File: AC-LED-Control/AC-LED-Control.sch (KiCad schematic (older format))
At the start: 44 parts, among them P101 CONN_01X02, P102 CONN_01X02, P103 CONN_01X04, P104 CONN_01X02, SW101 SW_PUSH, U101 FOD814-D, U102 STM32F030F4P6, U103 74HC595, U104 74HC595

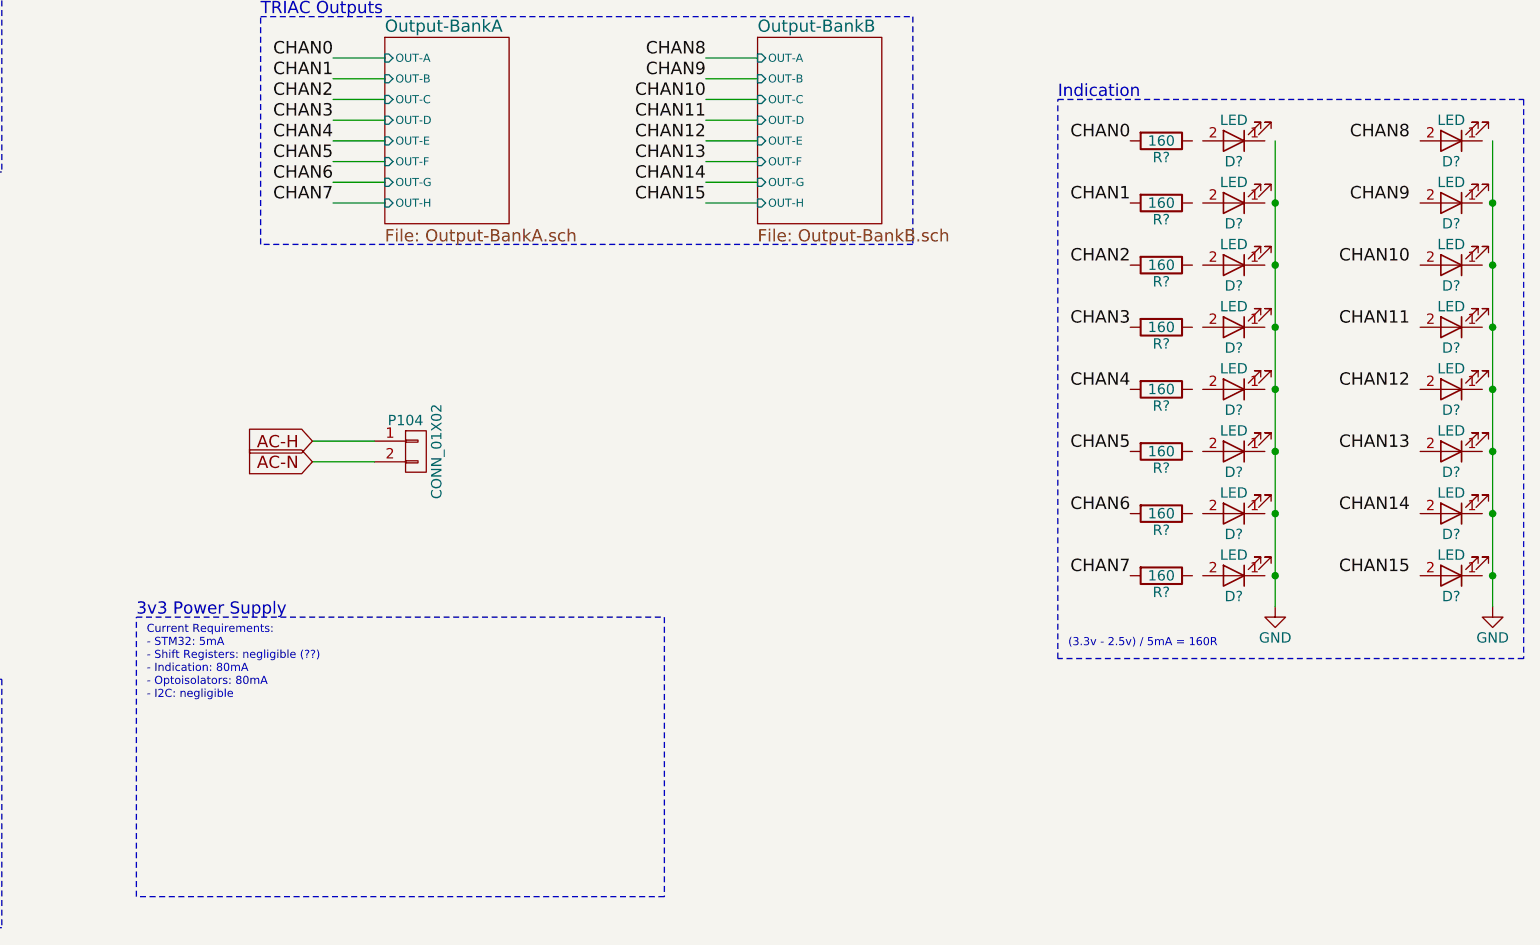
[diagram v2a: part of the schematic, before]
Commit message: Added 3v3 power regulator
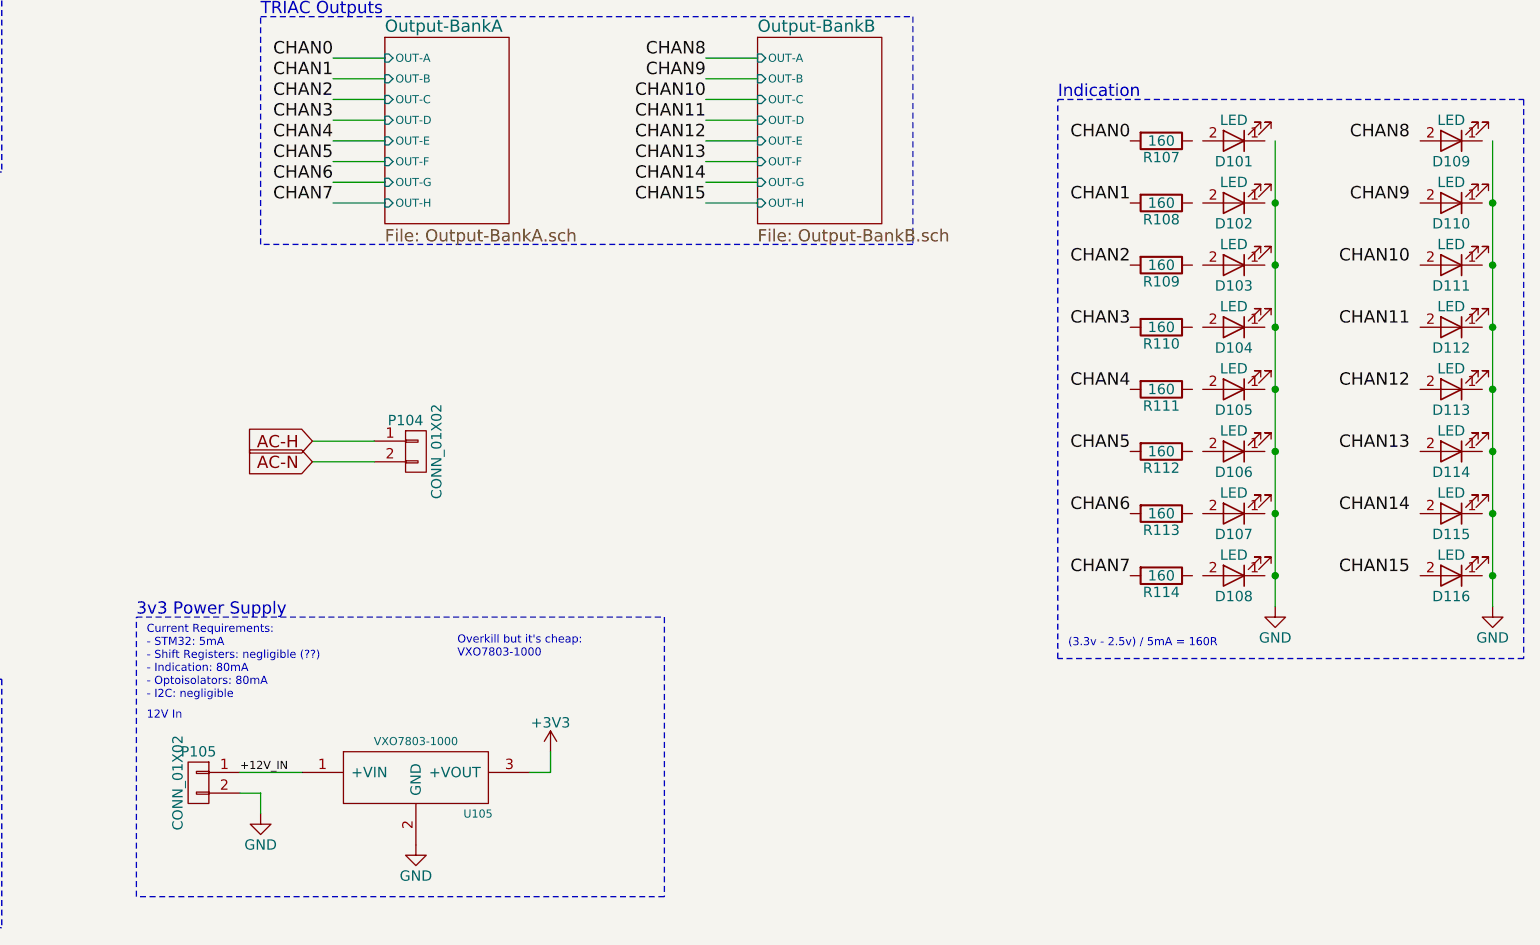
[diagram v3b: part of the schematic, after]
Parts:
- added P105: CONN_01X02, symbol CONN_01X02
- added U105: VXO7803-1000, symbol VXO7803-1000
- gave numbers to parts that had none: 24
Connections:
- net labels added: +12V_IN
- wire segments 54 -> 59
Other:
- note added: "12V In"
- note added: "Overkill but it's cheap:\nVXO7803-1000"

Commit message: Associated LEDs
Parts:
- D101, D102, D103, D104, D105, D106, D107, D108, D109, D110, D111, D112, D113, D114, D115, D116: footprint (none) -> LEDs:LED_0805
- R107, R108, R109, R110, R111, R112, R113, R114: footprint (none) -> Resistors_SMD:R_0603_HandSoldering
- U105: footprint (none) -> power_reg:VXO7803-1000

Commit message: Changed up isolation scheme and added BOM
Instead of isolating each of the TRIAC channels individually,
I changed it so the system uses an isolated power supply and isolates
itself from I2C as well.

Basic BOM was started as well.
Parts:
- removed P101, P102: CONN_01X02, Pin_Headers:Pin_Header_Straight_1x02, symbol CONN_01X02
- removed U105: VXO7803-1000, power_reg:VXO7803-1000, symbol VXO7803-1000
- added J? (x2): Conn_01x03, symbol Conn_01x03
- added P?: CONN_01X02, symbol CONN_01X02
- added R? (x2): 660, symbol R
- added U?: IE1203S, symbol IE1203S
- added U?: LTV-827, Housings_DIP:DIP-8_W7.62mm, symbol LTV-827
- D101, D102, D103, D104, D105, D106, D107, D108, D109, D110, D111, D112, D113, D114, D115, D116: symbol LED -> LED-RESCUE-AC-LED-Control
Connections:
- net +12V_IN: now also U?.1 (+VIN)
- net +3V3: now also R?.2, R?.2, U?.4 (+VOUT); no longer R104.1, R105.1
- net CHAN10: now also D111.2 (A)
- net CHAN11: now also D112.2 (A)
- net CHAN12: now also D113.2 (A)
- net CHAN13: now also D114.2 (A)
- net CHAN14: now also D115.2 (A)
- net CHAN15: now also D116.2 (A)
- net CHAN8: now also D109.2 (A)
- net CHAN9: now also D110.2 (A)
- net GND: now also D101.1 (K), D102.1 (K), D103.1 (K), D104.1 (K), D105.1 (K), D106.1 (K), D107.1 (K), D108.1 (K), D109.1 (K), D110.1 (K), D111.1 (K), D112.1 (K), D113.1 (K), D114.1 (K), D115.1 (K), D116.1 (K), U?.2, U?.3 (-VOUT), U?.4; no longer P105.2 (P2)
- net I2C_SCL: now also J?.1 (Pin_1), J?.1 (Pin_1), U?.8; no longer U102.17 (PA9)
- net I2C_SDA: now also J?.2 (Pin_2), J?.2 (Pin_2), U?.6; no longer U102.18 (PA10)
- net at R107.1: now also D101.2 (A)
- net at R108.1: now also D102.2 (A)
- net at R109.1: now also D103.2 (A)
- net at R110.1: now also D104.2 (A)
- net at R111.1: now also D105.2 (A)
- net at R112.1: now also D106.2 (A)
- net at R113.1: now also D107.2 (A)
- net at R114.1: now also D108.2 (A)
- new net 3v3_ISO: R104.1, R105.1
- new net 3v_ISO: P?.1 (P1)
- new net GND_IN: J?.3 (Pin_3), J?.3 (Pin_3), P105.2 (P2), P?.2 (P2), U?.2 (-VIN), U?.5, U?.7
- new net STM_SCL: R?.1, U102.17 (PA9), U?.1
- new net STM_SDA: R?.1, U102.18 (PA10), U?.3
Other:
- note added: "General Design Notes:\n- Anything touching AC should be isolated.\n- System is isolated from it's 12V power supply.\n- I2C is isolated."
- note added: "I2C"
- note added: "I2C is isolated, so there needs to be either:\na) other pullups\nb) other 3v3 power supply"
- note added: "Need isolation, found this:\nBT136S-600D,118"
- note removed: "I2C Connectors\n"
- note removed: "I2C Pullups do not have \nto be populated\nif pullups exist elsewhere."
- note removed: "Overkill but it's cheap:\nVXO7803-1000"
- moved on the sheet: P104, R103, R104, R105, SW101, U103, U104

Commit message: Modified some values for finding components
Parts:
- J101, J102: renamed from J?; footprint (none) -> Pin_Headers:Pin_Header_Straight_1x03_Pitch2.54mm
- P101: renamed from P?; footprint (none) -> Pin_Headers:Pin_Header_Straight_1x02_Pitch2.54mm
- P104, P105: footprint (none) -> Pin_Headers:Pin_Header_Straight_1x02_Pitch2.54mm
- R103: value 10K -> 16K
- R115, R116: renamed from R?; value 660 -> 680; footprint (none) -> Resistors_SMD:R_0603_HandSoldering
- gave numbers to parts that had none: 2
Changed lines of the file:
@@
 	1400 1750 1400 1850
 $Comp
-L GND #PWR02
+L GND #PWR01
 U 1 1 5B454DB5
 P 1400 1850
-F 0 "#PWR02" H 1400 1600 50  0001 C CNN
+F 0 "#PWR01" H 1400 1600 50  0001 C CNN
 F 1 "GND" H 1400 1700 50  0000 C CNN
 F 2 "" H 1400 1850 50  0000 C CNN
@@
 $EndComp
 $Comp
-L GND #PWR03
+L GND #PWR02
 U 1 1 5B454DF7
 P 1650 2900
-F 0 "#PWR03" H 1650 2650 50  0001 C CNN
+F 0 "#PWR02" H 1650 2650 50  0001 C CNN
 F 1 "GND" H 1650 2750 50  0000 C CNN
 F 2 "" H 1650 2900 50  0000 C CNN
@@
 $EndComp
 $Comp
-L GND #PWR04
+L GND #PWR03
 U 1 1 5B454F8F
 P 1350 3600
-F 0 "#PWR04" H 1350 3350 50  0001 C CNN
+F 0 "#PWR03" H 1350 3350 50  0001 C CNN
 F 1 "GND" H 1350 3450 50  0000 C CNN
 F 2 "" H 1350 3600 50  0000 C CNN
@@
 	7250 1100 7250 950
 $Comp
-L +3V3 #PWR05
+L +3V3 #PWR04
 U 1 1 5B455E79
 P 7250 950
-F 0 "#PWR05" H 7250 800 50  0001 C CNN
+F 0 "#PWR04" H 7250 800 50  0001 C CNN
 F 1 "+3V3" H 7250 1090 50  0000 C CNN
 F 2 "" H 7250 950 50  0000 C CNN
@@
 	7250 2200 7250 2350
 $Comp
-L GND #PWR06
+L GND #PWR05
 U 1 1 5B455F67
 P 7250 2350
-F 0 "#PWR06" H 7250 2100 50  0001 C CNN
+F 0 "#PWR05" H 7250 2100 50  0001 C CNN
 F 1 "GND" H 7250 2200 50  0000 C CNN
 F 2 "" H 7250 2350 50  0000 C CNN
@@
 	4650 1100 4650 950
 $Comp
-L +3V3 #PWR07
+L +3V3 #PWR06
 U 1 1 5B456028
 P 4650 950
-F 0 "#PWR07" H 4650 800 50  0001 C CNN
+F 0 "#PWR06" H 4650 800 50  0001 C CNN
 F 1 "+3V3" H 4650 1090 50  0000 C CNN
 F 2 "" H 4650 950 50  0000 C CNN
@@
 	4650 2200 4650 2350
 $Comp
-L GND #PWR08
+L GND #PWR07
 U 1 1 5B4560F7
 P 4650 2350
-F 0 "#PWR08" H 4650 2100 50  0001 C CNN
+F 0 "#PWR07" H 4650 2100 50  0001 C CNN
 F 1 "GND" H 4650 2200 50  0000 C CNN
 F 2 "" H 4650 2350 50  0000 C CNN
@@
 	850  4750 850  4650
 $Comp
-L +3V3 #PWR09
+L +3V3 #PWR08
 U 1 1 5B4571F5
 P 850 4350
-F 0 "#PWR09" H 850 4200 50  0001 C CNN
+F 0 "#PWR08" H 850 4200 50  0001 C CNN
 F 1 "+3V3" H 850 4490 50  0000 C CNN
 F 2 "" H 850 4350 50  0000 C CNN
@@
 P 850 4500
 F 0 "R103" V 930 4500 50  0000 C CNN
-F 1 "10K" V 850 4500 50  0000 C CNN
+F 1 "16K" V 850 4500 50  0000 C CNN
 F 2 "Resistors_SMD:R_0603_HandSoldering" V 780 4500 50  0001 C CNN
 F 3 "" H 850 4500 50  0000 C CNN
@@
 $EndComp
 $Comp
-L GND #PWR010
+L GND #PWR09
 U 1 1 5B4575F8
 P 850 5350
-F 0 "#PWR010" H 850 5100 50  0001 C CNN
+F 0 "#PWR09" H 850 5100 50  0001 C CNN
 F 1 "GND" H 850 5200 50  0000 C CNN
 F 2 "" H 850 5350 50  0000 C CNN
@@
 	800  1000 800  1250
 $Comp
-L GND #PWR011
+L GND #PWR010
 U 1 1 5B45876A
 P 800 1250
-F 0 "#PWR011" H 800 1000 50  0001 C CNN
+F 0 "#PWR010" H 800 1000 50  0001 C CNN
 F 1 "GND" H 800 1100 50  0000 C CNN
 F 2 "" H 800 1250 50  0000 C CNN
@@
 	3300 2800 3300 2700
 $Comp
-L +3V3 #PWR012
+L +3V3 #PWR011
 U 1 1 5B4593A7
 P 3300 2700
-F 0 "#PWR012" H 3300 2550 50  0001 C CNN
+F 0 "#PWR011" H 3300 2550 50  0001 C CNN
 F 1 "+3V3" H 3300 2840 50  0000 C CNN
 F 2 "" H 3300 2700 50  0000 C CNN
@@
 	2900 2900 2900 3000
 $Comp
-L GND #PWR013
+L GND #PWR012
 U 1 1 5B459412
 P 2900 3000
-F 0 "#PWR013" H 2900 2750 50  0001 C CNN
+F 0 "#PWR012" H 2900 2750 50  0001 C CNN
 F 1 "GND" H 2900 2850 50  0000 C CNN
 F 2 "" H 2900 3000 50  0000 C CNN
@@
 $EndComp
 $Comp
-L +3V3 #PWR014
+L +3V3 #PWR013
 U 1 1 5B463D3E
 P 2650 6500
-F 0 "#PWR014" H 2650 6350 50  0001 C CNN
+F 0 "#PWR013" H 2650 6350 50  0001 C CNN
 F 1 "+3V3" H 2650 6640 50  0000 C CNN
 F 2 "" H 2650 6500 50  0000 C CNN
@@
 	2650 7200 2650 7300
 $Comp
-L GND #PWR015
+L GND #PWR014
 U 1 1 5B464157
 P 2650 7300
-F 0 "#PWR015" H 2650 7050 50  0001 C CNN
+F 0 "#PWR014" H 2650 7050 50  0001 C CNN
 F 1 "GND" H 2650 7150 50  0000 C CNN
 F 2 "" H 2650 7300 50  0000 C CNN
@@
 Connection ~ 1150 1650
 $Comp
-L +3V3 #PWR016
+L +3V3 #PWR015
 U 1 1 5B465D50
 P 950 1650
-F 0 "#PWR016" H 950 1500 50  0001 C CNN
+F 0 "#PWR015" H 950 1500 50  0001 C CNN
 F 1 "+3V3" H 950 1790 50  0000 C CNN
 F 2 "" H 950 1650 50  0000 C CNN
@@
 F 0 "P104" H 7550 4800 50  0000 C CNN
 F 1 "CONN_01X02" V 7700 4650 50  0000 C CNN
-F 2 "" H 7600 4650 50  0001 C CNN
+F 2 "Pin_Headers:Pin_Header_Straight_1x02_Pitch2.54mm" H 7600 4650 50  0001 C CNN
 F 3 "" H 7600 4650 50  0000 C CNN
 	1    7600 4650
@@
 	9650 3700 9650 5950
 $Comp
-L GND #PWR017
+L GND #PWR016
 U 1 1 5B48AF70
 P 9650 5950
-F 0 "#PWR017" H 9650 5700 50  0001 C CNN
+F 0 "#PWR016" H 9650 5700 50  0001 C CNN
 F 1 "GND" H 9650 5800 50  0000 C CNN
 F 2 "" H 9650 5950 50  0000 C CNN
@@
 	10700 3700 10700 5950
 $Comp
-L GND #PWR018
+L GND #PWR017
 U 1 1 5B48B7DB
 P 10700 5950
-F 0 "#PWR018" H 10700 5700 50  0001 C CNN
+F 0 "#PWR017" H 10700 5700 50  0001 C CNN
 F 1 "GND" H 10700 5800 50  0000 C CNN
 F 2 "" H 10700 5950 50  0000 C CNN
@@
 Need isolation, found this:\nBT136S-600D,118
 $Comp
-L +3V3 #PWR020
+L +3V3 #PWR018
 U 1 1 5B49AE2D
 P 6150 6650
-F 0 "#PWR020" H 6150 6500 50  0001 C CNN
+F 0 "#PWR018" H 6150 6500 50  0001 C CNN
 F 1 "+3V3" H 6150 6790 50  0000 C CNN
 F 2 "" H 6150 6650 50  0000 C CNN
@@
 F 0 "P105" H 4450 6950 50  0000 C CNN
 F 1 "CONN_01X02" V 4550 6800 50  0000 C CNN
-F 2 "" H 4450 6800 50  0001 C CNN
+F 2 "Pin_Headers:Pin_Header_Straight_1x02_Pitch2.54mm" H 4450 6800 50  0001 C CNN
 F 3 "" H 4450 6800 50  0000 C CNN
 	1    4450 6800
@@
 S 5800 2900 600  900
 U 5B5700D7
-F0 "Output-BankA" 59
-F1 "Output-BankA.sch" 59
+F0 "Output-BankB" 59
+F1 "Output-BankB.sch" 59
 F2 "OUT-A" I L 5800 3000 39
 F3 "OUT-B" I L 5800 3100 39
@@
 $EndSheet
 $Comp
-L IE1203S U?
+L IE1203S U106
 U 1 1 5B571F37
 P 5500 6750
-F 0 "U?" H 5500 6550 59  0000 C CNN
+F 0 "U106" H 5500 6550 59  0000 C CNN
 F 1 "IE1203S" H 5500 6850 59  0000 C CNN
-F 2 "" H 5500 6750 39  0000 C CNN
+F 2 "" H 5500 6750 39  0001 C CNN
 F 3 "" H 5500 6750 39  0000 C CNN
 	1    5500 6750
@@
 	6050 6850 6150 6850
 $Comp
-L GND #PWR?
+L GND #PWR019
 U 1 1 5B572609
 P 6150 6950
-F 0 "#PWR?" H 6150 6700 50  0001 C CNN
+F 0 "#PWR019" H 6150 6700 50  0001 C CNN
 F 1 "GND" H 6150 6800 50  0000 C CNN
 F 2 "" H 6150 6950 50  0001 C CNN
@@
 3v3_ISO
 $Comp
-L CONN_01X02 P?
+L CONN_01X02 P101
 U 1 1 5B57404C
 P 2300 4350
-F 0 "P?" H 2300 4500 50  0000 C CNN
+F 0 "P101" H 2300 4500 50  0000 C CNN
 F 1 "CONN_01X02" V 2400 4350 50  0000 C CNN
-F 2 "" H 2300 4350 50  0000 C CNN
+F 2 "Pin_Headers:Pin_Header_Straight_1x02_Pitch2.54mm" H 2300 4350 50  0001 C CNN
 F 3 "" H 2300 4350 50  0000 C CNN
 	1    2300 4350
@@
 	2800 5600 2800 4100
 $Comp
-L Conn_01x03 J?
+L Conn_01x03 J101
 U 1 1 5B57569C
 P 6300 4750
-F 0 "J?" H 6300 4950 50  0000 C CNN
+F 0 "J101" H 6300 4950 50  0000 C CNN
 F 1 "Conn_01x03" H 6300 4550 50  0000 C CNN
-F 2 "" H 6300 4750 50  0001 C CNN
+F 2 "Pin_Headers:Pin_Header_Straight_1x03_Pitch2.54mm" H 6300 4750 50  0001 C CNN
 F 3 "" H 6300 4750 50  0001 C CNN
 	1    6300 4750
@@
 $EndComp
 $Comp
-L Conn_01x03 J?
+L Conn_01x03 J102
 U 1 1 5B5757A9
 P 6300 5300
-F 0 "J?" H 6300 5500 50  0000 C CNN
+F 0 "J102" H 6300 5500 50  0000 C CNN
 F 1 "Conn_01x03" H 6300 5100 50  0000 C CNN
-F 2 "" H 6300 5300 50  0001 C CNN
+F 2 "Pin_Headers:Pin_Header_Straight_1x03_Pitch2.54mm" H 6300 5300 50  0001 C CNN
 F 3 "" H 6300 5300 50  0001 C CNN
 	1    6300 5300
@@
 STM_SDA
 $Comp
-L LTV-827 U?
+L LTV-827 U105
 U 1 1 5B5788E8
 P 4950 5250
-F 0 "U?" H 4750 5650 50  0000 L CNN
+F 0 "U105" H 4750 5650 50  0000 L CNN
 F 1 "LTV-827" H 4950 5650 50  0000 L CNN
 F 2 "Housings_DIP:DIP-8_W7.62mm" H 4750 4900 50  0001 L CIN
@@
 I2C
 $Comp
-L R R?
+L R R115
 U 1 1 5B57907C
 P 4050 4750
-F 0 "R?" V 4130 4750 50  0000 C CNN
-F 1 "660" V 4050 4750 50  0000 C CNN
-F 2 "" V 3980 4750 50  0001 C CNN
+F 0 "R115" V 4130 4750 50  0000 C CNN
+F 1 "680" V 4050 4750 50  0000 C CNN
+F 2 "Resistors_SMD:R_0603_HandSoldering" V 3980 4750 50  0001 C CNN
 F 3 "" H 4050 4750 50  0001 C CNN
 	1    4050 4750
@@
 $EndComp
 $Comp
-L R R?
+L R R116
 U 1 1 5B579225
 P 4300 4750
-F 0 "R?" V 4380 4750 50  0000 C CNN
-F 1 "660" V 4300 4750 50  0000 C CNN
-F 2 "" V 4230 4750 50  0001 C CNN
+F 0 "R116" V 4380 4750 50  0000 C CNN
+F 1 "680" V 4300 4750 50  0000 C CNN
+F 2 "Resistors_SMD:R_0603_HandSoldering" V 4230 4750 50  0001 C CNN
 F 3 "" H 4300 4750 50  0001 C CNN
 	1    4300 4750
@@
 	3450 4450 3450 5650
 $Comp
-L GND #PWR?
+L GND #PWR020
 U 1 1 5B57B922
 P 4500 5450
-F 0 "#PWR?" H 4500 5200 50  0001 C CNN
+F 0 "#PWR020" H 4500 5200 50  0001 C CNN
 F 1 "GND" H 4500 5300 50  0000 C CNN
 F 2 "" H 4500 5450 50  0001 C CNN
@@
 Connection ~ 4050 4600
 $Comp
-L +3V3 #PWR?
+L +3V3 #PWR021
 U 1 1 5B57CBCB
 P 3850 4600
-F 0 "#PWR?" H 3850 4450 50  0001 C CNN
+F 0 "#PWR021" H 3850 4450 50  0001 C CNN
 F 1 "+3V3" H 3850 4740 50  0000 C CNN
 F 2 "" H 3850 4600 50  0001 C CNN

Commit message: Finished final associations and tweaks
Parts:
- removed D101, D102, D103, D104, D105, D106, D107, D108, D109, D110, D111, D112, D113, D114, D115, D116: LED, LEDs:LED_0805, symbol LED-RESCUE-AC-LED-Control
- removed P101: CONN_01X02, Pin_Headers:Pin_Header_Straight_1x02_Pitch2.54mm, symbol CONN_01X02
- added D101, D102, D103, D104, D105, D106, D107, D108, D109, D110, D111, D112, D113, D114, D115, D116: LED, LEDs:LED_0603_HandSoldering, symbol LED
- added J103: Conn_01x02, Pin_Headers:Pin_Header_Straight_1x02_Pitch2.54mm, symbol Conn_01x02
- SW101: footprint Buttons_Switches_SMD:SW_SPST_EVPBF -> Buttons_Switches_THT:SW_PUSH_6mm_h5mm
- U106: footprint (none) -> SIP-Packages:SIP-4
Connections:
- net 3v_ISO: now also J103.2 (Pin_2)
- net CHAN10: now also D106.2 (A)
- net CHAN11: now also D108.2 (A)
- net CHAN12: now also D110.2 (A)
- net CHAN13: now also D112.2 (A)
- net CHAN14: now also D114.2 (A)
- net CHAN15: now also D116.2 (A)
- net CHAN8: now also D102.2 (A)
- net CHAN9: now also D104.2 (A)
- net GND: now also D101.1 (K), D102.1 (K), D103.1 (K), D104.1 (K), D105.1 (K), D106.1 (K), D107.1 (K), D108.1 (K), D109.1 (K), D110.1 (K), D111.1 (K), D112.1 (K), D113.1 (K), D114.1 (K), D115.1 (K), D116.1 (K)
- net GND_IN: now also J103.1 (Pin_1)
- net at R107.1: now also D101.2 (A)
- net at R108.1: now also D103.2 (A)
- net at R109.1: now also D105.2 (A)
- net at R110.1: now also D107.2 (A)
- net at R111.1: now also D109.2 (A)
- net at R112.1: now also D111.2 (A)
- net at R113.1: now also D113.2 (A)
- net at R114.1: now also D115.2 (A)
